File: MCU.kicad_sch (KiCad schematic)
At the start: 41 parts, among them J15 Conn_01x08, J16 Conn_02x04_Odd_Even, J17 Conn_01x04_MountingPin, J19 Conn_01x04_MountingPin, SW1 SW_Push_Dual, SW2 SW_Push_Dual, SW3 SW_DIP_x08, U15 MCP1700-3302E_SOT23, U16 CD74HC4067M, U17 MCP2562FD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

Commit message: Routing WIP
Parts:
- Q13: value (none) -> SI2300; footprint (none) -> Package_TO_SOT_SMD:SOT-23
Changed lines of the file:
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@@
       (effects (font (size 1.27 1.27)) hide)
     )
-    (property "Value" "" (id 1) (at 209.55 266.573 0))
+    (property "Value" "GNDA" (id 1) (at 209.55 266.573 0))
     (property "Footprint" "" (id 2) (at 209.55 261.493 0)
       (effects (font (size 1.27 1.27)) hide)
@@
       (effects (font (size 1.27 1.27)) (justify left))
     )
-    (property "Value" "" (id 1) (at 212.471 256.0319 0)
-      (effects (font (size 1.27 1.27)) (justify left))
-    )
-    (property "Footprint" "" (id 2) (at 212.09 256.667 0)
+    (property "Value" "SI2300" (id 1) (at 212.471 256.0319 0)
+      (effects (font (size 1.27 1.27)) (justify left))
+    )
+    (property "Footprint" "Package_TO_SOT_SMD:SOT-23" (id 2) (at 212.09 256.667 0)
       (effects (font (size 1.27 1.27) italic) (justify left) hide)
     )

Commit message: Layout WIP
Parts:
- D14, D15, D16, D17: footprint LED_THT:LED_D1.8mm_W3.3mm_H2.4mm -> (none)
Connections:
- net DEBUG_LED: now also U19.19 (PA5); no longer U19.46 (PB15)
- net INPUT_SELECT: now also U19.46 (PB15); no longer U19.19 (PA5)
- net MUX2_~{EN}: now also U19.72 (PB3); no longer U19.78 (PB9)
- net Speaker_1: now also U19.78 (PB9); no longer U19.72 (PB3)
- net GND1: now reaches SW3.9
- net GND1: now also U16.23 (I8); no longer U16.16 (I15)
- net GND2: now reaches SW3.10
- net GND2: now also U16.22 (I9); no longer U16.17 (I14)
- net GND3: now reaches SW3.11
- net GND3: now also U16.21 (I10); no longer U16.18 (I13)
- net GND4: now reaches SW3.12
- net GND4: now also U16.20 (I11); no longer U16.19 (I12)
- net GND5: now reaches SW3.13
- net GND5: now also U16.19 (I12); no longer U16.20 (I11)
- net GND6: now reaches SW3.14
- net GND6: now also U16.18 (I13); no longer U16.21 (I10)
- net GND7: now reaches SW3.15
- net GND7: now also U16.17 (I14); no longer U16.22 (I9)
- net GND8: now reaches SW3.16
- net GND8: now also U16.16 (I15); no longer U16.23 (I8)

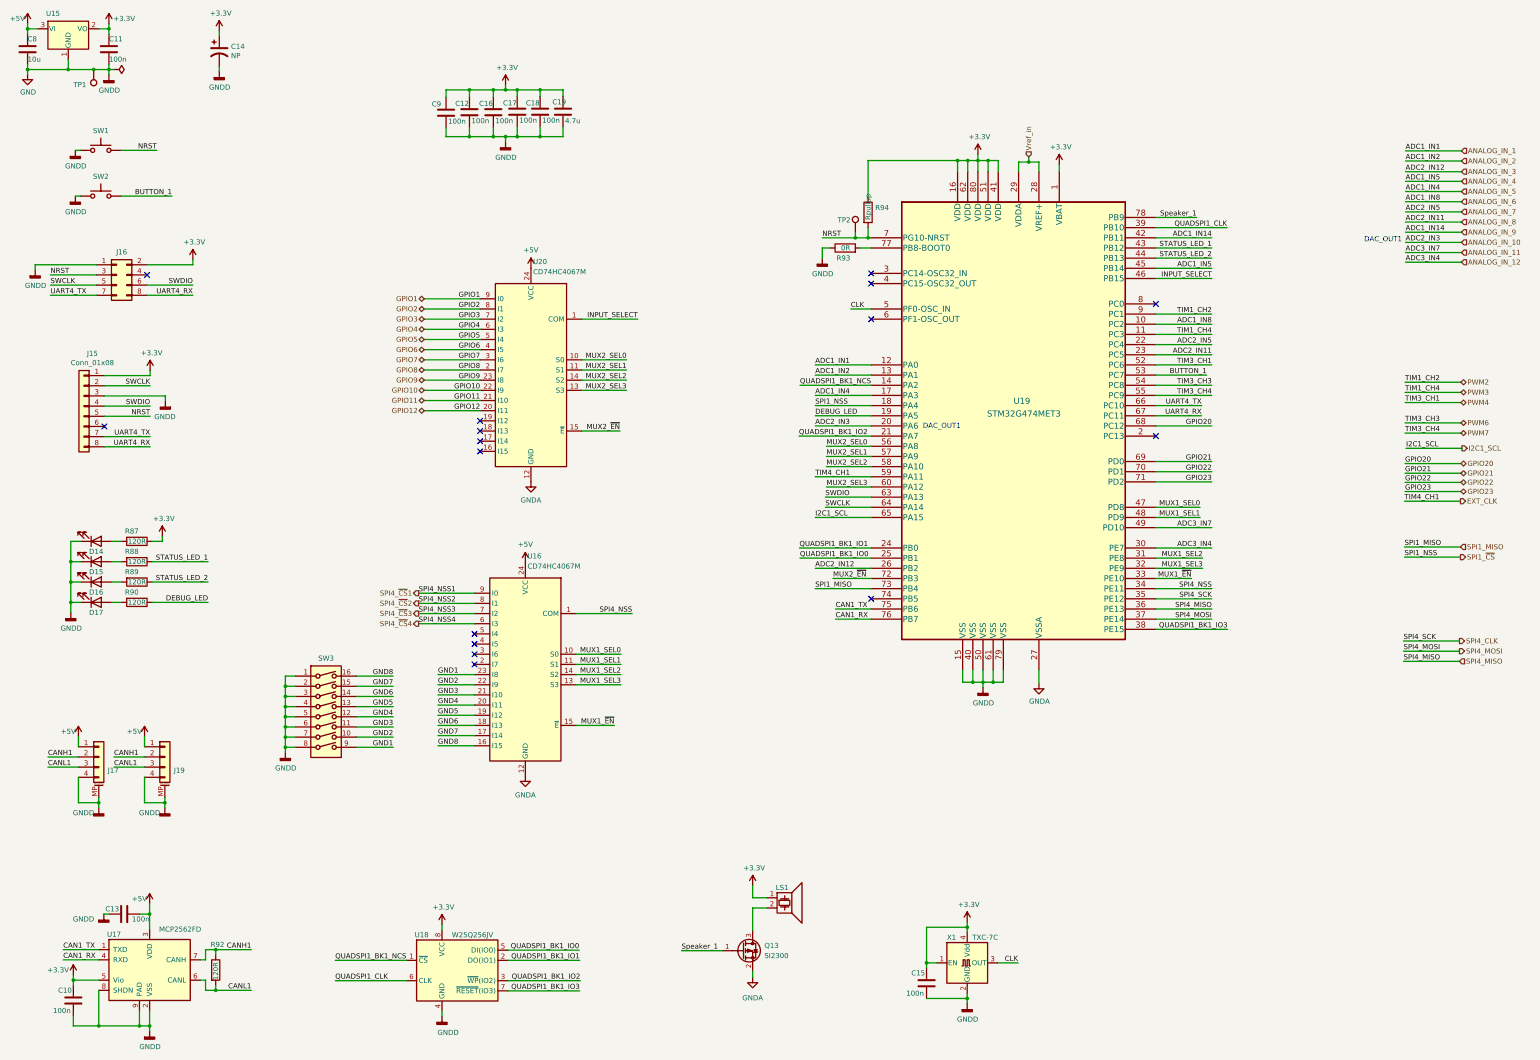
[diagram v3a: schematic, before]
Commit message: Connectors change and part side flip
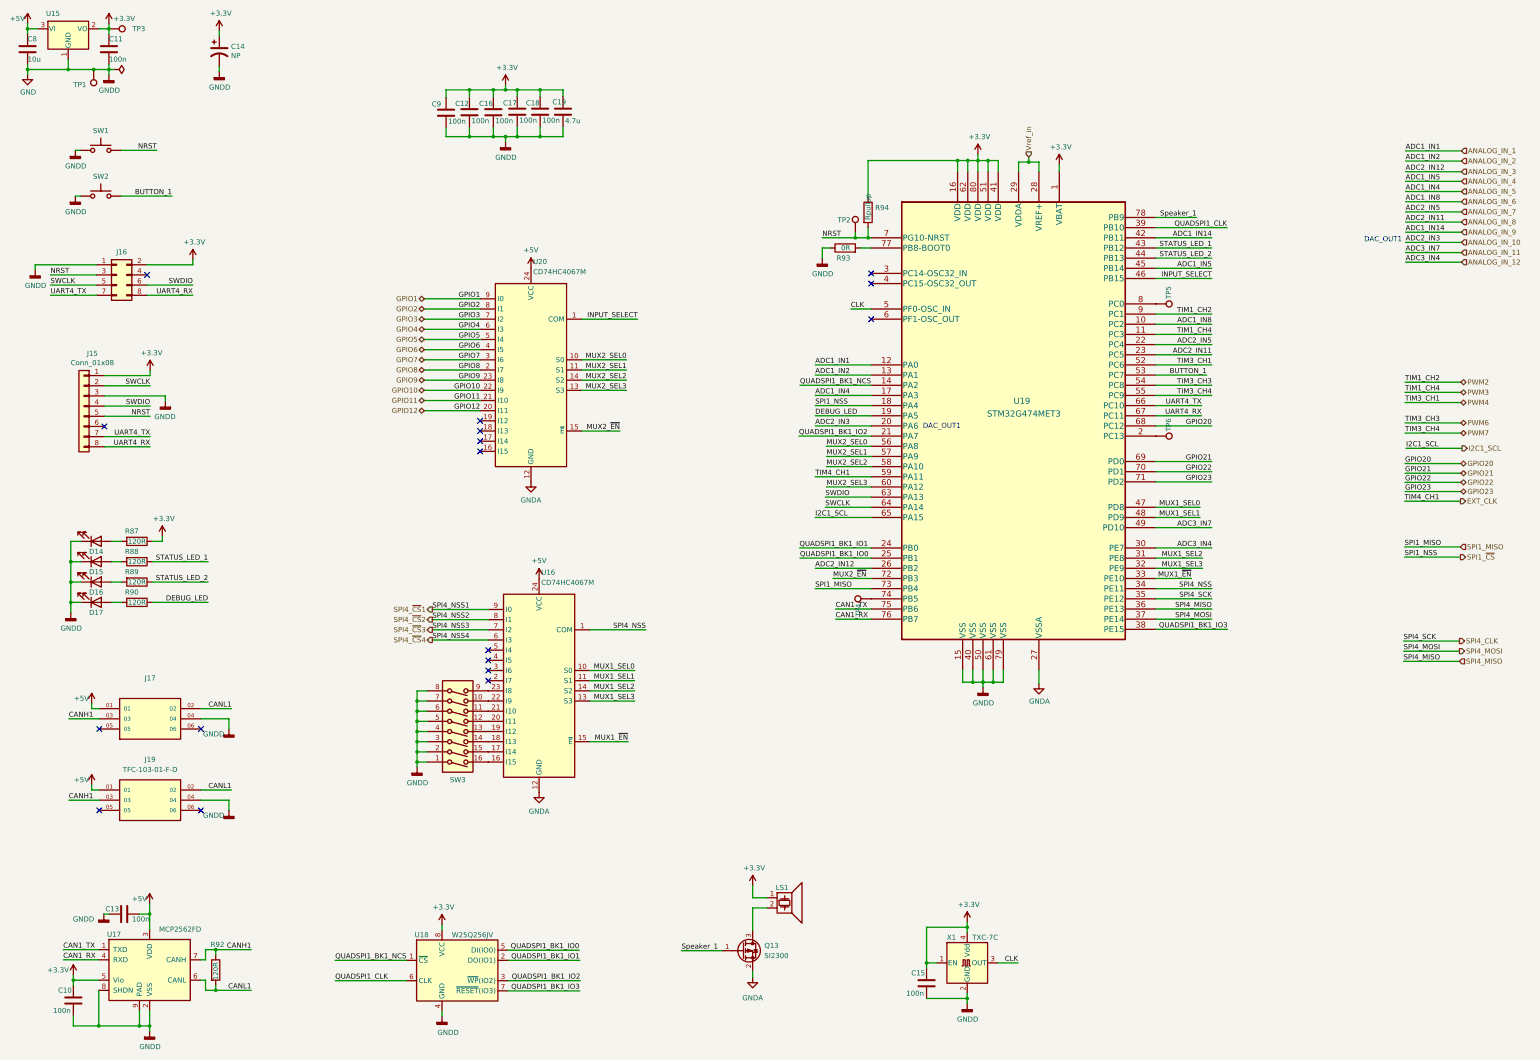
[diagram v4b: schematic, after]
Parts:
- removed J17, J19: Conn_01x04_MountingPin, Connector_JST:JST_GH_BM04B-GHS-TBT_1x04-1MP_P1.25mm_Vertical, symbol Connector_Generic_MountingPin:Conn_01x04_MountingPin
- added J17: (no value), symbol TFC-103-01-F-D:TFC-103-01-F-D
- added J19: TFC-103-01-F-D, SAMTEC_TFC-103-01-F-D, symbol TFC-103-01-F-D:TFC-103-01-F-D
- added TP3, TP4, TP5, TP6: TestPoint, TestPoint:TestPoint_THTPad_D1.0mm_Drill0.5mm, symbol Connector:TestPoint
- D14, D15, D16, D17: footprint (none) -> LED_SMD:LED_0603_1608Metric
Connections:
- net +3V3: now also TP3.1
- net +5V: now also J17.01, J19.01
- net CANH1: now also J17.03, J19.03
- net CANL1: now also J17.02, J19.02
- net GND: now also J17.04, J19.04
- net at U19.2 (PC13): now also TP6.1
- net at U19.74 (PB5): now also TP4.1
- net at U19.8 (PC0): now also TP5.1
- net GND1: no longer names the net of SW3.9, U16.23 (I8)
- net GND2: no longer names the net of SW3.10, U16.22 (I9)
- net GND3: no longer names the net of SW3.11, U16.21 (I10)
- net GND4: no longer names the net of SW3.12, U16.20 (I11)
- net GND5: no longer names the net of SW3.13, U16.19 (I12)
- net GND6: no longer names the net of SW3.14, U16.18 (I13)
- net GND7: no longer names the net of SW3.15, U16.17 (I14)
- net GND8: no longer names the net of SW3.16, U16.16 (I15)
- no-connect marks 16 -> 17
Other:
- moved on the sheet: SW3, U16

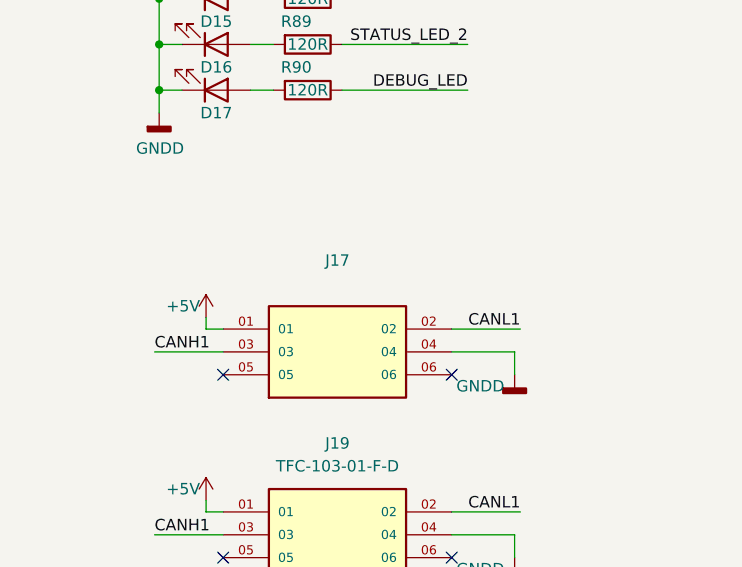
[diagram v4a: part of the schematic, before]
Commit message: Connectors routed
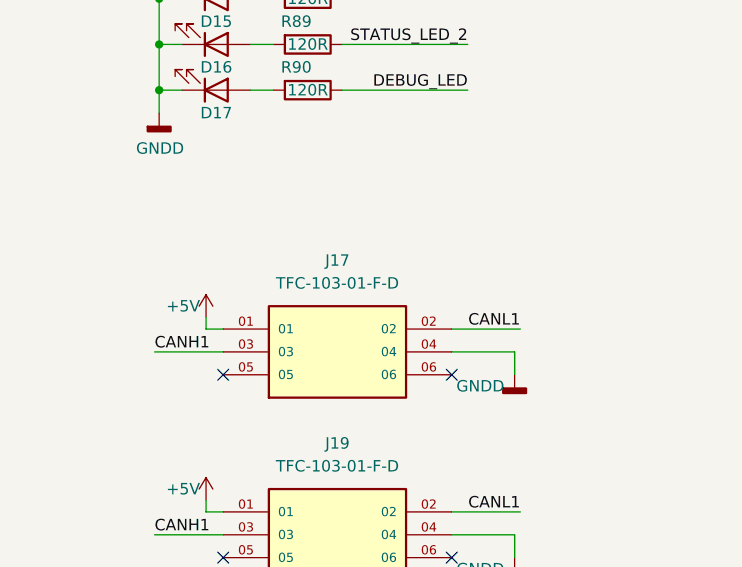
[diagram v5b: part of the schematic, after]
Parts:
- J17: value (none) -> TFC-103-01-F-D; footprint (none) -> SAMTEC_TFC-103-01-F-D
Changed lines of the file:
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@@
     (in_bom yes) (on_board yes) (fields_autoplaced)
     (property "Reference" "J17" (id 0) (at 59.055 186.69 0))
-    (property "Value" "" (id 1) (at 59.055 189.23 0))
-    (property "Footprint" "" (id 2) (at 59.055 196.85 0)
+    (property "Value" "TFC-103-01-F-D" (id 1) (at 59.055 189.23 0))
+    (property "Footprint" "SAMTEC_TFC-103-01-F-D" (id 2) (at 59.055 196.85 0)
       (effects (font (size 1.27 1.27)) (justify bottom) hide)
     )

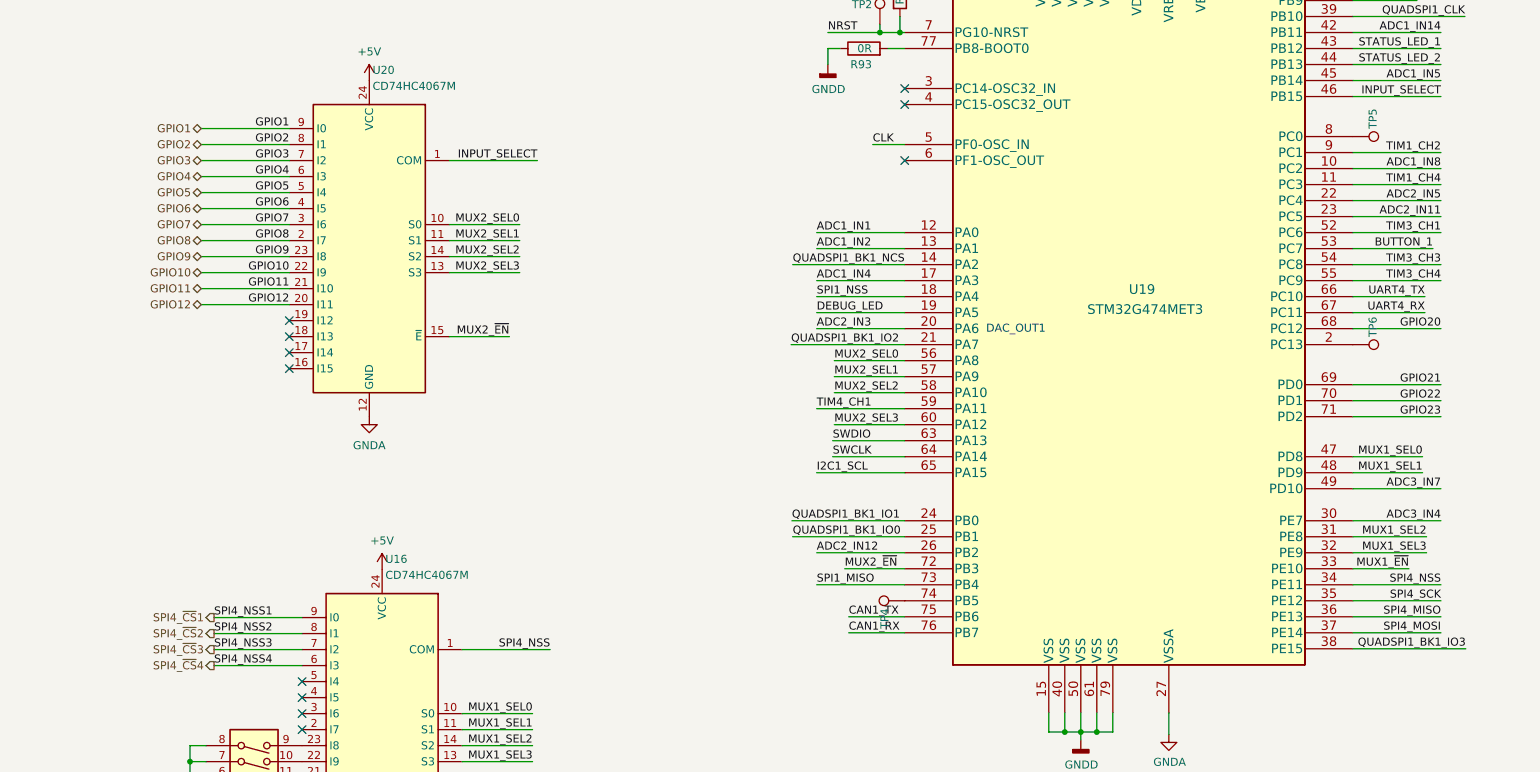
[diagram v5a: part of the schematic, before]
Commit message: Routing basics done
All layers + the basic layout is already set
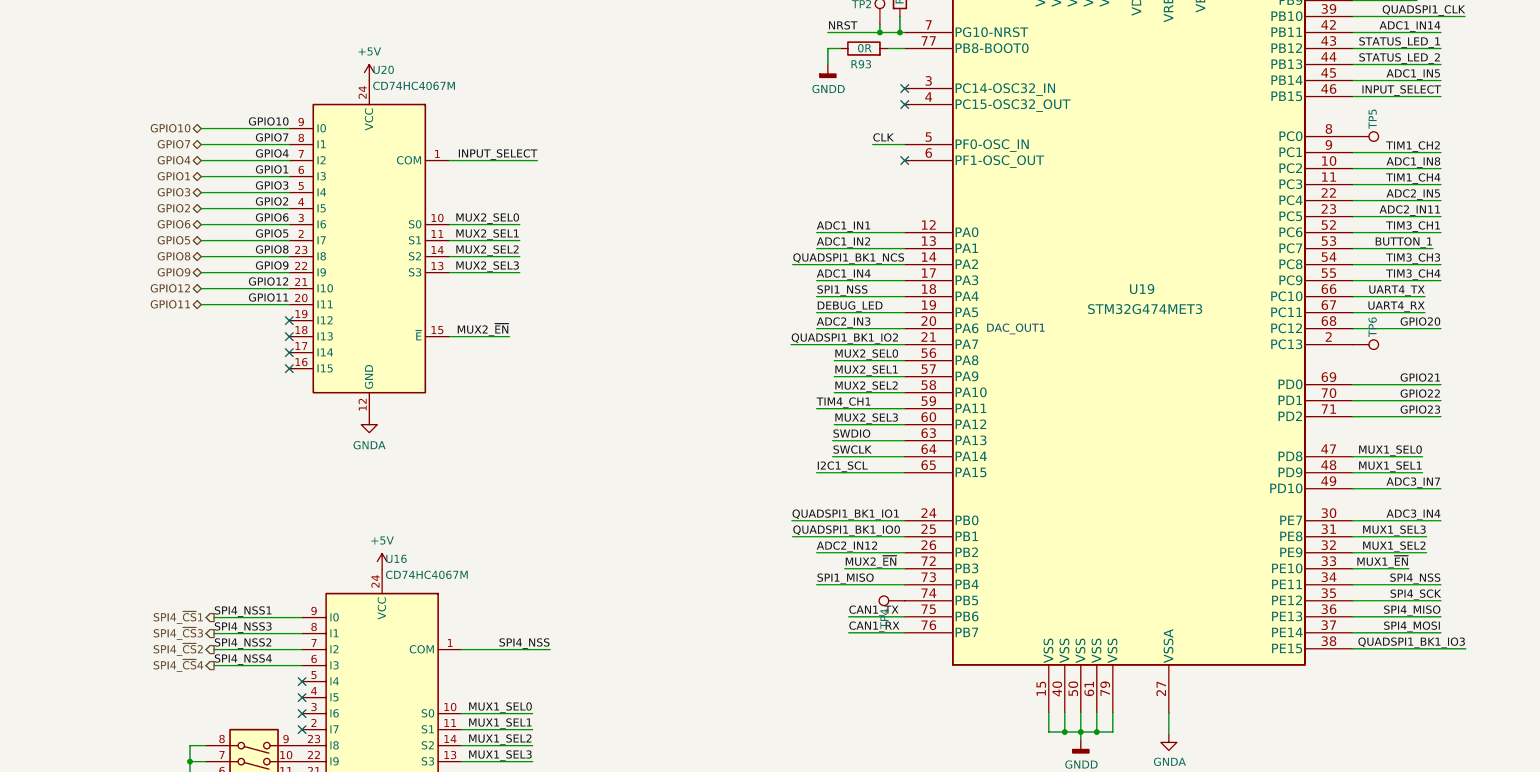
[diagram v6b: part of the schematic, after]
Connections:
- net GPIO1: now also U20.6 (I3); no longer U20.9 (I0)
- net GPIO10: now also U20.9 (I0); no longer U20.22 (I9)
- net GPIO11: now also U20.20 (I11); no longer U20.21 (I10)
- net GPIO12: now also U20.21 (I10); no longer U20.20 (I11)
- net GPIO2: now also U20.4 (I5); no longer U20.8 (I1)
- net GPIO3: now also U20.5 (I4); no longer U20.7 (I2)
- net GPIO4: now also U20.7 (I2); no longer U20.6 (I3)
- net GPIO5: now also U20.2 (I7); no longer U20.5 (I4)
- net GPIO6: now also U20.3 (I6); no longer U20.4 (I5)
- net GPIO7: now also U20.8 (I1); no longer U20.3 (I6)
- net GPIO8: now also U20.23 (I8); no longer U20.2 (I7)
- net GPIO9: now also U20.22 (I9); no longer U20.23 (I8)
- net MUX1_SEL2: now also U19.32 (PE9); no longer U19.31 (PE8)
- net MUX1_SEL3: now also U19.31 (PE8); no longer U19.32 (PE9)
- net SPI4_~{CS}2: now also U16.7 (I2); no longer U16.8 (I1)
- net SPI4_~{CS}3: now also U16.8 (I1); no longer U16.7 (I2)

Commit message: Routing WIP
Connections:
- net ANALOG_IN_12: now also U19.23 (PC5); no longer U19.30 (PE7)
- net ANALOG_IN_6: now also U19.30 (PE7); no longer U19.10 (PC2)
- net ANALOG_IN_7: now also U19.42 (PB11); no longer U19.22 (PC4)
- net ANALOG_IN_8: now also U19.10 (PC2); no longer U19.23 (PC5)
- net ANALOG_IN_9: now also U19.22 (PC4); no longer U19.42 (PB11)
- net EXT_CLK: now also U19.46 (PB15); no longer U19.59 (PA11)
- net GPIO20: now also U19.69 (PD0); no longer U19.68 (PC12)
- net GPIO21: now also U19.52 (PC6); no longer U19.69 (PD0)
- net GPIO22: now also U19.57 (PA9); no longer U19.70 (PD1)
- net GPIO23: now also U19.56 (PA8); no longer U19.71 (PD2)
- net I2C1_SCL: now also U19.58 (PA10); no longer U19.65 (PA15)
- net INPUT_SELECT: now also U19.59 (PA11); no longer U19.46 (PB15)
- net MUX1_SEL0: now also U19.44 (PB13); no longer U19.47 (PD8)
- net MUX1_SEL1: now also U19.43 (PB12); no longer U19.48 (PD9)
- net MUX2_SEL0: now also U19.65 (PA15); no longer U19.56 (PA8)
- net MUX2_SEL1: now also U19.68 (PC12); no longer U19.57 (PA9)
- net MUX2_SEL2: now also U19.73 (PB4); no longer U19.58 (PA10)
- net MUX2_SEL3: now also U19.72 (PB3); no longer U19.60 (PA12)
- net MUX2_~{EN}: now also U19.74 (PB5); no longer U19.72 (PB3)
- net PWM4: now also U19.70 (PD1); no longer U19.52 (PC6)
- net SPI1_MISO: now also U19.71 (PD2); no longer U19.73 (PB4)
- net SPI1_~{CS}: now also U19.8 (PC0); no longer U19.18 (PA4)
- net STATUS_LED_1: now also U19.47 (PD8); no longer U19.43 (PB12)
- net STATUS_LED_2: now also U19.48 (PD9); no longer U19.44 (PB13)
- net Speaker_1: now also U19.60 (PA12); no longer U19.78 (PB9)
- net at TP4.1: now also U19.78 (PB9); no longer U19.74 (PB5)
- net at TP5.1: now also U19.18 (PA4); no longer U19.8 (PC0)
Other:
- moved on the sheet: R93, R94, TP2, TP6, U19
